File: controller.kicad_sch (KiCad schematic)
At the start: 1 part, among them U1 STM32G473CBT3

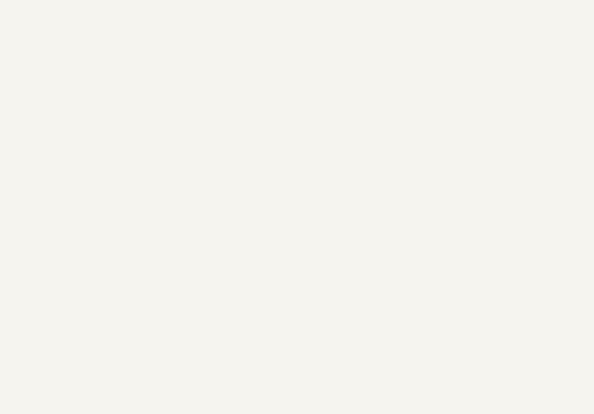
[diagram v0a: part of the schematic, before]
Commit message: Added power domain stuff
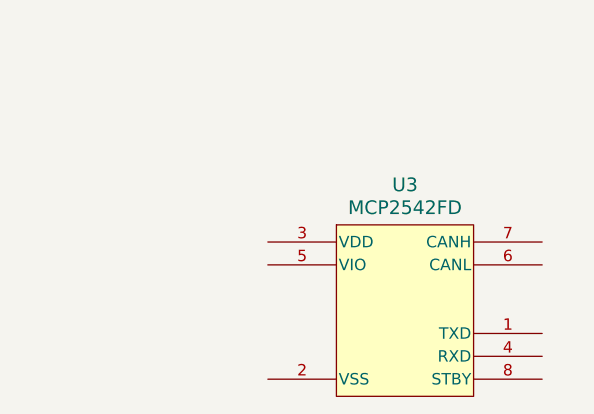
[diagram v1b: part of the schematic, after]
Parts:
- added U3: MCP2542FD, Sullivan-Labs:SOIC8_4P9X3P9MC_MCH, symbol Sullivan-Labs:IC MCP2542FD CAN Transceiver
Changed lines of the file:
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@@
+	)
+	(symbol
+		(lib_id "Sullivan-Labs:IC MCP2542FD CAN Transceiver")
+		(at 203.2 124.46 0)
+		(unit 1)
+		(exclude_from_sim no)
+		(in_bom yes)
+		(on_board yes)
+		(dnp no)
+		(fields_autoplaced yes)
+		(property "Reference" "U3"
+			(at 218.44 118.11 0)
+			(effects
+				(font
+					(size 1.524 1.524)
+				)
+			)
+		)
+		(property "Value" "MCP2542FD"
+			(at 218.44 120.65 0)
+			(effects
+				(font
+					(size 1.524 1.524)
+				)
+			)
+		)
+		(property "Footprint" "Sullivan-Labs:SOIC8_4P9X3P9MC_MCH"
+			(at 209.042 152.908 0)
+			(effects
+				(font
+					(size 1.27 1.27)
+					(italic yes)
+				)
+				(hide yes)
+			)
+		)
+		(property "Datasheet" ""
+			(at 203.2 124.46 0)
+			(effects
+				(font
+					(size 1.27 1.27)
+					(italic yes)
+				)
+				(hide yes)
+			)
+		)
+		(property "Description" "CAN Transceiver with VIO"
+			(at 208.026 145.034 0)
+			(effects
+				(font
+					(size 1.27 1.27)
+				)
+				(hide yes)
+			)
+		)
+		(property "Manufacturer" "Microchip Technology"
+			(at 208.28 146.05 0)
+			(effects
+				(font
+					(size 1.27 1.27)
+				)
+				(hide yes)
+			)
+		)
+		(property "PN" "MCP2542FD-E/SN"
+			(at 208.534 145.288 0)
+			(effects
+				(font
+					(size 1.27 1.27)
+				)
+				(hide yes)
+			)
+		)
+		(pin "1"
+		)
+		(pin "4"
+		)
+		(pin "3"
+		)
+		(pin "2"
+		)
+		(pin "5"
+		)
+		(pin "8"
+		)
+		(pin "7"
+		)
+		(pin "6"
+		)
+		(instances
+			(project ""
+				(path "/d013d610-c58f-4b11-9d18-37fc135ac516/ddbda7f4-3933-4f27-89fe-4c477c945179"
+					(reference "U3")
+					(unit 1)
+				)
+			)
+		)
 	)
 	(symbol

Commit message: Small changes to schematic
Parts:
- removed U3: MCP2542FD, Sullivan-Labs:SOIC8_4P9X3P9MC_MCH, symbol Sullivan-Labs:IC MCP2542FD CAN Transceiver
- added C30, C31, C32, C33: .1uF 25V, Sullivan-Labs:C_0402_1005Metric, symbol Sullivan-Labs:CAP_.1uF_25V_0402
- added C34, C35, C36, C37: 470pF 50V, Sullivan-Labs:C_0402_1005Metric, symbol Sullivan-Labs:CAP_470pF_50V_0402
- added D4: ESD8708MUTAG, Sullivan-Labs:UDFN14_517CN_ONS, symbol Sullivan-Labs:DIODE 8-CH TVS 3.3V
- added D5: Green, Sullivan-Labs:LED_SML-D12V1WT86, symbol Sullivan-Labs:LED Green-Yellow 20mA 2.2Vf
- added FB3, FB4: 440mA 600ohm, Sullivan-Labs:R_0402_1005Metric, symbol Sullivan-Labs:FB_600Ohm_100MHz_0402
- added J3: ST-LINK, Sullivan-Labs:SAMTEC_FTSH-107-01-F-DV-K-P, symbol Sullivan-Labs:CONN ST-LINK 14pos 0.050{dblquote} (1.27mm)
- added R36, R38, R41: 0R, Sullivan-Labs:R_0402_1005Metric, symbol Sullivan-Labs:RES_0R_0402
- added R37: 1.5k, Sullivan-Labs:R_0603_1608Metric, symbol Sullivan-Labs:RES_1.5k_0603
- added R39: 150R, Sullivan-Labs:R_0603_1608Metric, symbol Sullivan-Labs:RES_150R_0603
- added R42: 10k, Sullivan-Labs:R_0402_1005Metric, symbol Sullivan-Labs:RES_10k_0402
- added TP2, TP3: TestPoint, Sullivan-Labs:TestPoint_Pad_D1.0mm, symbol Sullivan-Labs:TP 1mm Circle
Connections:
- net VDD: now reaches U1.1 (VBAT)
- net VDD: now also U1.24 (VDD), U1.36 (VDD), U1.48 (VDD), C30.1, C32.1, C33.1, C35.1, C36.1, C37.1, FB3.2, R37.2, R42.1
- net GND: now reaches U1.19 (VSSA)
- net GND: now also U1.23 (VSS), U1.35 (VSS), U1.47 (VSS), C30.2, C31.2, C32.2, C33.2, C34.2, C35.2, C36.2, C37.2, D4.3, D4.6, D4.9, J3.5 (GND), J3.7 (GND)
- net VDDA: now reaches U1.20 (VREF+)
- net VDDA: now also U1.21 (VDDA), C31.1, C34.1, FB4.2
- net UART_RX: now reaches U1.32 (PA10)
- net UART_RX: now also R36.1
- net JTMS: now reaches U1.37 (PA13)
- net JTMS: now also D4.10, J3.4 (JTMS/SWDIO)
- net JTCK: now reaches U1.38 (PA14)
- net JTCK: now also D4.8, J3.6 (JCLK/SWCLK)
- net JTDI: now reaches U1.39 (PA15)
- net JTDI: now also D4.7, J3.10 (JTDI)
- net JTDO: now reaches U1.40 (PB3)
- net JTDO: now also D4.5, J3.8 (JTDO/SWO)
- net UART_TX: now reaches U1.43 (PB6)
- net UART_TX: now also R38.2
- net at U1.44 (PB7): now also R41.2
- net CAN_RX: now reaches U1.45 (PB8-BOOT0)
- net CAN_RX: now also TP2.1
- net CAN_TX: now reaches U1.46 (PB9)
- net CAN_TX: now also TP3.1
- net NRST: now reaches U1.7 (PG10-NRST)
- net NRST: now also D4.2, J3.12 (NRST), R42.2
- new net: D5.C, R39.1
- new net: J3.3 (T_VCC), R37.1
- new net +3.3V: D5.A, FB3.1, FB4.1
- new net RX: D4.11, J3.13 (VCP_RX), R36.2
- new net STATUS: R39.2
- new net STBY: R41.1
- new net TX: D4.1, J3.14 (VCP_TX), R38.1
- no-connect marks 0 -> 8
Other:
- moved on the sheet: U1A, U1B

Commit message: Initial schematic is done
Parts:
- added D16, D17, D18, D19: Red, Sullivan-Labs:LED_SML-D12V1WT86, symbol Sullivan-Labs:LED Red 20mA 2.2Vf
- added R52: 0R, Sullivan-Labs:R_0402_1005Metric, symbol Sullivan-Labs:RES_0R_0402
- added R72, R73, R74, R75: 150R, Sullivan-Labs:R_0603_1608Metric, symbol Sullivan-Labs:RES_150R_0603
- added TP7: TestPoint, Sullivan-Labs:TestPoint_Pad_D1.0mm, symbol Sullivan-Labs:TP 1mm Circle
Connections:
- net +3.3V: now also D16.A, D17.A, D18.A, D19.A
- net GND: now also R52.2; no longer U1.19 (VSSA)
- net STATUS: now also U1.2 (PC13)
- net EN2: now reaches U1.10 (PA2)
- net EN3: now reaches U1.11 (PA3)
- net FAULT0: now reaches U1.12 (PA4)
- net GAUGE_CTRL: now reaches U1.13 (PA5)
- net FAULT1: now reaches U1.14 (PA6)
- net FAULT2: now reaches U1.15 (PA7)
- net VBATT: now reaches U1.16 (PB0)
- net SNS2: now reaches U1.17 (PB1)
- net EN0: now reaches U1.18 (PB2)
- net TEMP_CTRL: now reaches U1.22 (PB10)
- net SNS3: now reaches U1.25 (PB11)
- net SNS1: now reaches U1.26 (PB12)
- net at U1.27 (PB13): now also TP7.1
- net LP_EN0: now reaches U1.28 (PB14)
- net LP_EN1: now reaches U1.29 (PB15)
- net FAULT3: now reaches U1.30 (PA8)
- net OVERHEAT: now reaches U1.31 (PA9)
- net LED0: now reaches U1.33 (PA11)
- net LED0: now also R72.2
- net LED1: now reaches U1.34 (PA12)
- net LED1: now also R73.2
- net LED2: now reaches U1.41 (PB4)
- net LED2: now also R74.2
- net LED3: now reaches U1.42 (PB5)
- net LED3: now also R75.2
- net SNS0: now reaches U1.8 (PA0)
- net EN1: now reaches U1.9 (PA1)
- new net: D17.C, R73.1
- new net: D18.C, R74.1
- new net: D16.C, R72.1
- new net: D19.C, R75.1
- new net GNDA: R52.1, U1.19 (VSSA)
- no-connect marks 8 -> 7
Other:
- moved on the sheet: R42
